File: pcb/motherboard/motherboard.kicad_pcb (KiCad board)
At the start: 4 copper layers, 99.1 x 39.4 mm, 105 parts, among them J1 -, J10 PSU, J11 RESET-SW, J13 USB-LED, J14 EXT, J15 EXT-PW, J16 EXT-I2C, J17 WIFI-GPIO, J18 DB-C, J2 USB-MINI-B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

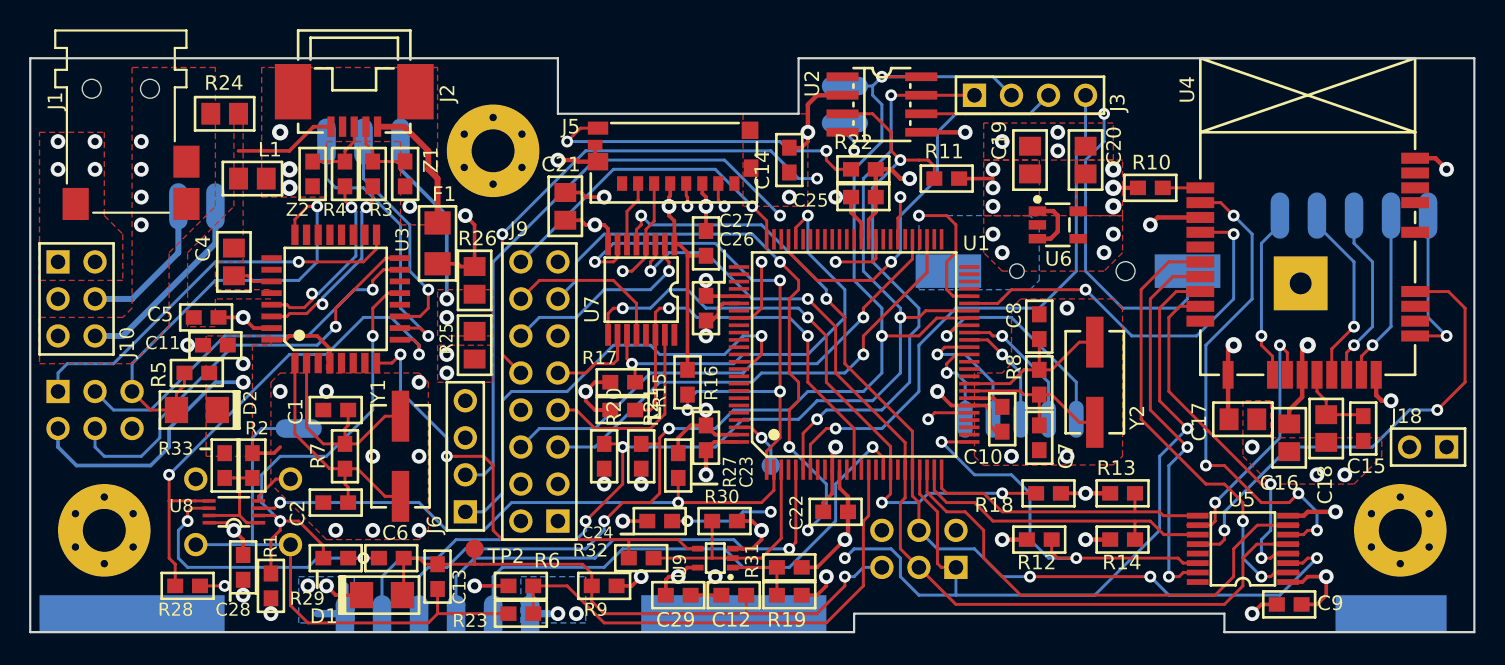
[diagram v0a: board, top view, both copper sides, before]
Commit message: Corrected solder mask clearance
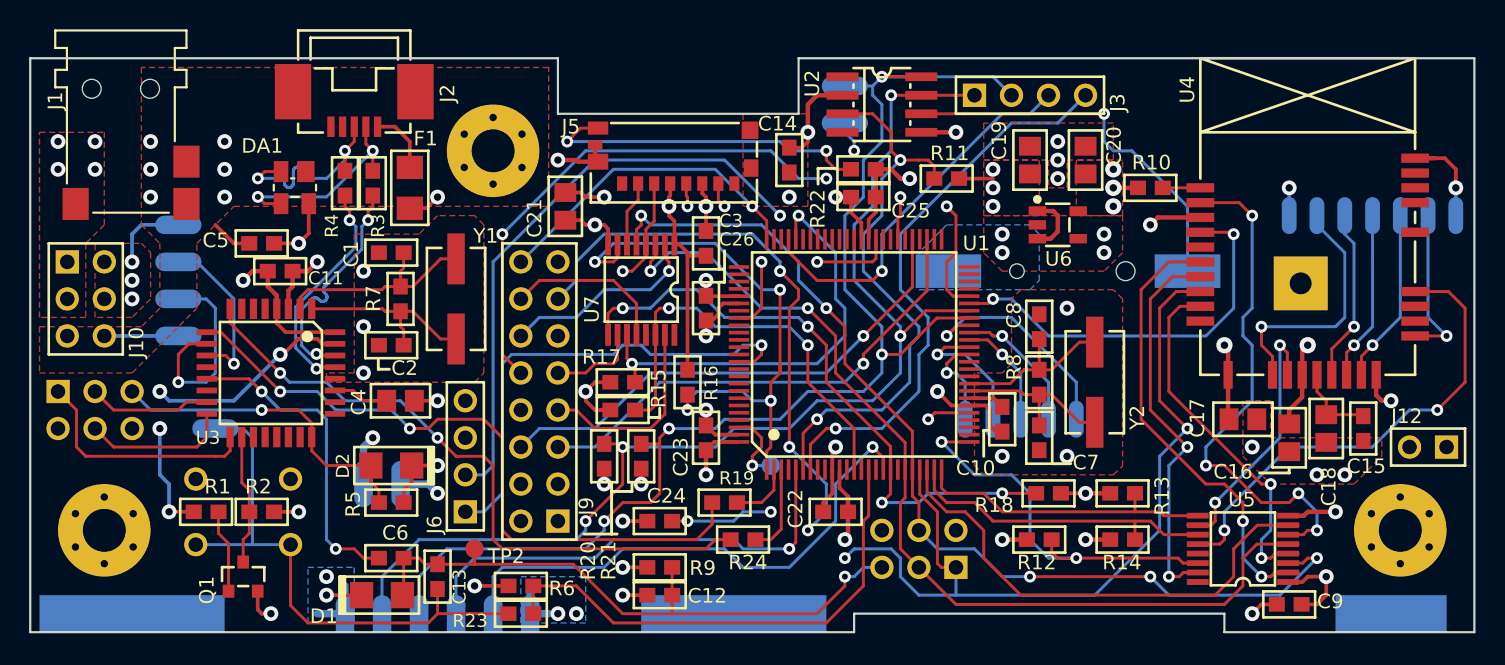
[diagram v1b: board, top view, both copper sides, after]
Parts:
- removed C28, C29: 100nF, smt:C-0603
- removed L1: BLM21, smt:FER-0805
- removed the R24 at (121.3, 88.3)
- removed R25: N/A, smt:R-0805
- removed R26: 0, smt:R-0805
- removed R27, R30: 10k, smt:R-0603
- removed R29, R32: N/A, smt:R-0603
- removed R31: 100k, smt:R-0603
- removed R33: 1k, smt:R-0603
- removed U8: 74LVC2G126DC, smt-sop:VSSOP8
- removed U9: 74AHC1G126SE-7, smt-sot:SOT-353
- removed Z1, Z2: CG0603MLC-05E, smt:FER-0603
- added DA1: SR05, smt-sot:SOT-143, F.Cu at (126.1, 93.3)
- added Q1: MMST3904, smt-sot:SOT23, F.Cu at (122.6, 120.0)
- added REF**: VAL**, symbols:LOGO-OSHW-250, B.Cu at (135.5, 101.9)
- F1: footprint smt:FER-1206 -> smt:R-1206
- J13: value USB-LED -> HEADER-1x04; footprint conn-wire-pads:WP-50mil-1x03 -> conn-wire-pads:WP-50mil-1x04
- J17: footprint conn-wire-pads:WP-50mil-1x05 -> conn-wire-pads:WP-40mil-1x07
- J4: value ICSP-0 -> ICSP
- J7: value ICSP-1 -> ICSP
- R2: value 100k -> 10k
- R24: renamed from R28; value N/A -> 1k
- moved R24 38.2 mm to (156.8, 117.5)
- moved J15 22.9 mm to (132.1, 113.7), turned to 180 degrees
- moved R5 16.0 mm to (132.7, 114.9)
- moved J13 15.9 mm to (118.1, 99.7), turned to 270 degrees
- moved C4 14.9 mm to (133.3, 108.0), turned to 180 degrees
- moved D2 13.9 mm to (132.7, 112.4)
- moved C2 11.4 mm to (132.7, 104.1)
- moved R7 11.4 mm to (133.3, 101.0)
- moved Y1 11.4 mm to (137.2, 101.0)
- moved C1 11.4 mm to (132.7, 97.8)
- moved R19 7.75 mm to (155.6, 114.9)
- moved R1 6.75 mm to (120.0, 115.6), turned to 0 degrees
- moved U3 6.75 mm to (124.5, 106.0), turned to 270 degrees
- moved C11 6.75 mm to (125.1, 99.1), turned to 0 degrees
- moved C5 6.35 mm to (123.8, 97.2)
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- renumbered C27 to C3, J18 to J12
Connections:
- C11 pad 1: UVCC -> +5V
- C16 pad 1: GND -> +3V3
- C16 pad 2: +3V3 -> GND
- C17 pad 1: GND -> +3V3
- C17 pad 2: +3V3 -> GND
- C3 pad 1: GND -> DVDD
- C3 pad 2: DVDD -> GND
- C4 pad 1: /USB Serial/UGND -> GND
- C5 pad 1: /USB Serial/UGND -> GND
- C5 pad 2: /USB Serial/UVCC_IN -> /USB Serial/UVCC
- C9 pad 1: GND -> +3V3
- C9 pad 2: +3V3 -> GND
- D2 pad K: UVCC -> +5V
- F1 pad 1: Net-(F1-Pad1) -> /USB Serial/UVCC_IN
- F1 pad 2: /USB Serial/UVCC_IN -> /USB Serial/UVCC
- J10 pad 2: /VIN -> +5V
- J10 pad 3: +5V -> /VIN
- J13 pad 1: UVCC -> +5V
- J17 pad 1: /Peripherals/GPIO_1 -> +3V3
- J17 pad 2: /Peripherals/GPIO_3 -> /Peripherals/GPIO_1
- J17 pad 3: /Peripherals/LED_WIFI -> /Peripherals/GPIO_3
- J17 pad 4: /Peripherals/LED_NET -> /Peripherals/LED_WIFI
- J17 pad 5: /Peripherals/LED_ERR -> /Peripherals/LED_NET
- J2 pad 1: Net-(F1-Pad1) -> /USB Serial/UVCC_IN
- J2 pad 5: /USB Serial/UGND -> GND
- J2 pad SH: /USB Serial/USHLD -> GND
- J4 pad 2: UVCC -> +5V
- R1 pad 1: /USB Serial/RESET-M -> /USB Serial/UVCC
- R1 pad 2: UVCC -> Net-(Q1-Pad1)
- R11 pad 1: +5V -> /RTC_INT
- R11 pad 2: /RTC_INT -> +5V
- R19 pad 1: Net-(R19-Pad1) -> /USB Serial/UTXD
- R19 pad 2: +5V -> /PE0
- R2 pad 1: GND -> +5V
- R2 pad 2: Net-(R2-Pad2) -> /USB Serial/VUSB-DET
- R24 pad 1: /USB Serial/UTXD -> /USB Serial/URXD
- R24 pad 2: /PE0 -> /PE1
- R5 pad 2: UVCC -> +5V
- U3 pad 13: /USB Serial/RESET-M -> /USB Serial/RESET
- U3 pad 18: Net-(U3-Pad18) -> /USB Serial/VUSB-DET
- U3 pad 28: /USB Serial/UGND -> GND
- U3 pad 31: /USB Serial/UVCC_IN -> /USB Serial/UVCC
- U3 pad 32: UVCC -> +5V
- U3 pad 4: UVCC -> +5V
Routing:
- net UVCC: track 91.3 -> 0.00 mm, vias 6 -> 0
- net /USB Serial/UVCC: track 0.00 -> 51.4 mm, vias 0 -> 6
- net /PE0: track 51.9 -> 4.30 mm, vias 3 -> 0
- net /USB Serial/RESET-M: track 32.4 -> 0.00 mm, vias 2 -> 0
- net /USB Serial/UVCC_IN: track 31.1 -> 5.17 mm, vias 2 -> 0
- net /USB Serial/MOSI-USB: track 29.6 -> 10.1 mm, vias 1 -> 0
- net /USB Serial/SCK-USB: track 25.8 -> 8.41 mm, vias 1 -> 0
- net GND: track 93.2 -> 81.5 mm, vias 48 -> 46
- net /USB Serial/URXD: track 33.9 -> 45.0 mm
- net /USB Serial/UTXD: track 35.7 -> 46.7 mm
- net /USB Serial/MISO-USB: track 28.9 -> 18.1 mm, vias 1 -> 0
- net /PE1: track 16.6 -> 6.15 mm
- net /USB Serial/D_IN+: track 4.88 -> 14.3 mm, vias 0 -> 2
- net /USB Serial/D_IN-: track 4.81 -> 14.2 mm, vias 0 -> 2
- net Net-(F1-Pad1): track 9.38 -> 0.00 mm
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- removed copper zone on F.Cu, net /USB Serial/UGND
- removed copper zone on F.Cu, net /USB Serial/USHLD
- removed copper zone on GND, net /USB Serial/USHLD
- removed copper zone on F.Cu, net UVCC
- removed copper zone on Power, net UVCC
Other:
- rule pad_to_mask_clearance: 0.1524 -> 0.1016
- board text added: "3.3V"
- board text added: "Alarm Clock v3"
- board text added: "ICSP0"
- board text added: "ICSP1"
- board text added: "REV. B"
- board text added: "RST"
- board text removed: "Alarm Clock V3"
- board text removed: "REV. A"
- board text removed: "UVCC"

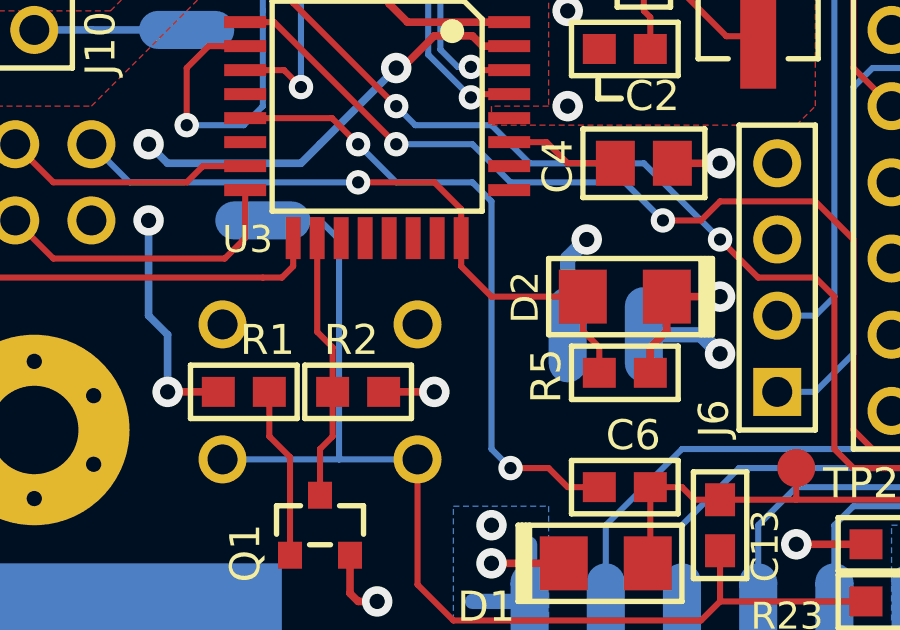
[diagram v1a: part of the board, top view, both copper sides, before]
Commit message: Changed pin for VUSB detection on U3
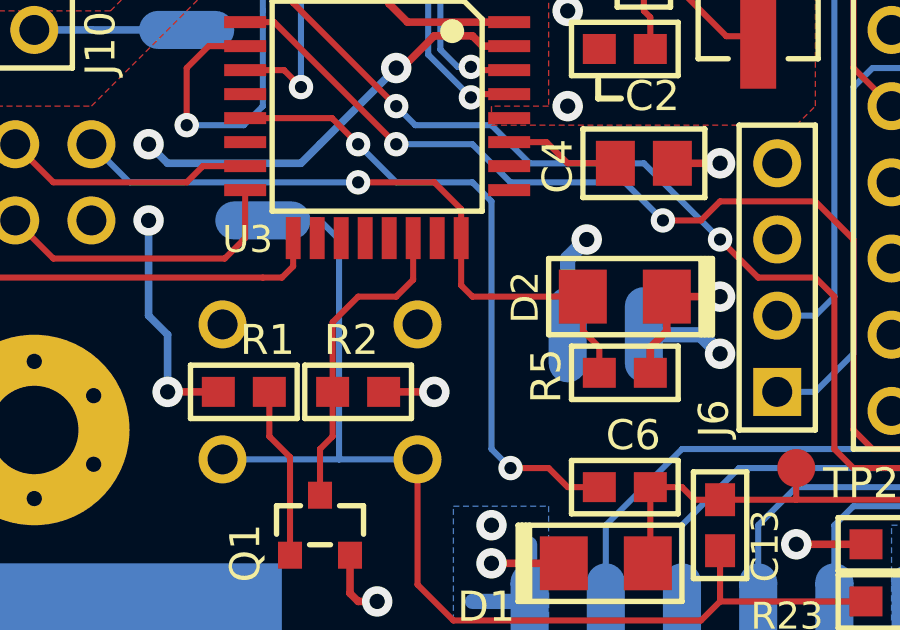
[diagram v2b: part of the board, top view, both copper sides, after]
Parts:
- J13: value HEADER-1x04 -> USB-LED
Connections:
- U3 pad 18: /USB Serial/VUSB-DET -> Net-(U3-Pad18)
- U3 pad 22: Net-(U3-Pad22) -> /USB Serial/VUSB-DET
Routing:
- net /USB Serial/VUSB-DET: track 8.96 -> 10.6 mm

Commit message: PSU board schematics/layout
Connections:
- net /LOW_BATT renamed /SYSOFF
